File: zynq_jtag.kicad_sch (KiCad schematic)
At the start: 79 parts, among them J300 Digilent HS2 Header, J301 USB-MICRO-B, Q300 T2N7002AK, SW300 SKRPANE010, SW301 219-3LPST, U300 FT2232HL-REEL, U301 93LC56BT-I/SN, U6 XC7Z020-2CLG400I, X300 12Mhz-TXC Corp

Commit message: ram-update
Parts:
- D300, D308, D309: footprint LED_0402_RED -> Footprint-Lib-PhilsLab:LED_0402_RED
- FB300, FB301, FB302: footprint FB_0402 -> Footprint-Lib-PhilsLab:FB_0402
- R310, R312, R314, R316, R319: footprint Resistor_SMD:R_0402_1005Metric -> easyeda2kicad_foorprint:R0201; LCSC C25765 -> C295787; Manufacturer Part Number 0402WGF2002TCE -> RC0201FR-0720KL
- SW300: footprint SKRPANE010 -> Footprint-Lib-PhilsLab:SKRPANE010

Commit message: ram-zynq-updated
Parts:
- D305: footprint Diode_SMD:D_SOD-323F -> easyeda2kicad_foorprint:SOD-323_L1.8-W1.3-LS2.5-RD
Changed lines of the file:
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@@
 			)
 		)
-		(property "Footprint" "Diode_SMD:D_SOD-323F"
+		(property "Footprint" "easyeda2kicad_foorprint:SOD-323_L1.8-W1.3-LS2.5-RD"
 			(at 307.34 67.945 0)
 			(effects

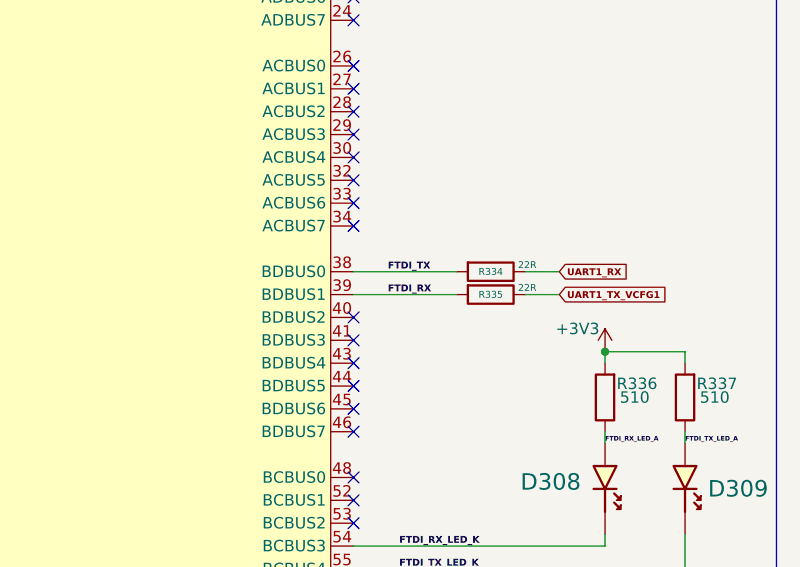
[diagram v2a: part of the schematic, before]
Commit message: usb hs update
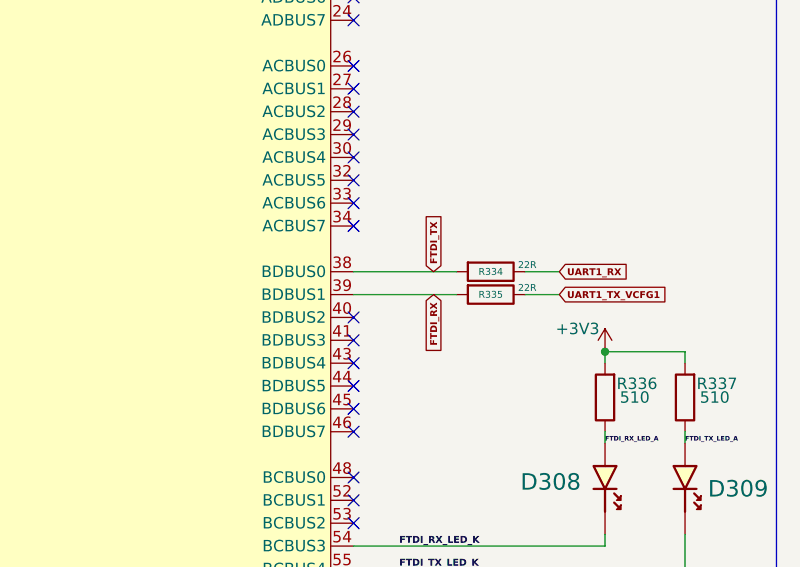
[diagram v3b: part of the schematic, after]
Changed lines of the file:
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@@
-	(wire
-		(pts
-			(xy 444.5 134.62) (xy 433.07 134.62)
-		)
-		(stroke
-			(width 0)
-			(type default)
-		)
-	)
 	(wire
 		(pts
@@
 		(pts
 			(xy 311.15 148.59) (xy 312.42 148.59)
+		)
+		(stroke
+			(width 0)
+			(type default)
+		)
+	)
+	(wire
+		(pts
+			(xy 433.07 134.62) (xy 444.5 134.62)
 		)
 		(stroke
@@
 		)
 	)
-	(label "FTDI_TX"
-		(at 436.88 132.08 0)
-		(fields_autoplaced yes)
-		(effects
-			(font
-				(size 0.762 0.762)
-				(thickness 0.254)
-				(bold yes)
-			)
-			(justify left bottom)
-		)
-	)
 	(label "USB_FTDI_D_N"
 		(at 311.15 104.14 0)
@@
 		)
 	)
-	(label "FTDI_RX"
-		(at 436.88 134.62 0)
-		(fields_autoplaced yes)
-		(effects
-			(font
-				(size 0.762 0.762)
-				(thickness 0.254)
-				(bold yes)
-			)
-			(justify left bottom)
-		)
-	)
 	(label "TMS_0"
 		(at 60.96 50.8 0)
@@
 			)
 			(justify left bottom)
+		)
+	)
+	(global_label "FTDI_RX"
+		(shape input)
+		(at 441.96 134.62 270)
+		(fields_autoplaced yes)
+		(effects
+			(font
+				(size 0.762 0.762)
+				(thickness 0.254)
+				(bold yes)
+			)
+			(justify right)
+		)
+		(property "Intersheetrefs" "${INTERSHEET_REFS}"
+			(at 441.96 141.3143 90)
+			(effects
+				(font
+					(size 1.27 1.27)
+				)
+				(justify right)
+				(hide yes)
+			)
 		)
 	)
@@
 			(effects
 				(font
+					(size 1.27 1.27)
+				)
+				(justify left)
+				(hide yes)
+			)
+		)
+	)
+	(global_label "FTDI_TX"
+		(shape input)
+		(at 441.96 132.08 90)
+		(fields_autoplaced yes)
+		(effects
+			(font
+				(size 0.762 0.762)
+				(thickness 0.254)
+				(bold yes)
+			)
+			(justify left)
+		)
+		(property "Intersheetrefs" "${INTERSHEET_REFS}"
+			(at 441.96 125.5671 90)
+			(effects
+				(font

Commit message: pcb layers
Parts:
- SW300: footprint Footprint-Lib-PhilsLab:SKRPANE010 -> easyeda2kicad_foorprint:SW-SMD_4P-L4.2-W3.2-P2.15-LS4.6-2
- U300: footprint Footprint-Lib-PhilsLab:LQFP-64-0.5mm -> easyeda2kicad_foorprint:LQFP-64_L10.0-W10.0-P0.50-LS12.0-TL
- U301: footprint Footprint-Lib-PhilsLab:SOIC-8 -> easyeda2kicad_foorprint:SOIC-8_L5.0-W4.0-P1.27-LS6.0-BL
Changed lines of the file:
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@@
 			)
 		)
-		(property "Footprint" "Footprint-Lib-PhilsLab:SOIC-8"
+		(property "Footprint" "easyeda2kicad_foorprint:SOIC-8_L5.0-W4.0-P1.27-LS6.0-BL"
 			(at 288.29 165.1 0)
 			(effects
@@
 			)
 		)
-		(property "Footprint" "Footprint-Lib-PhilsLab:LQFP-64-0.5mm"
+		(property "Footprint" "easyeda2kicad_foorprint:LQFP-64_L10.0-W10.0-P0.50-LS12.0-TL"
 			(at 392.43 134.62 0)
 			(effects
@@
 			)
 		)
-		(property "Footprint" "Footprint-Lib-PhilsLab:SKRPANE010"
+		(property "Footprint" "easyeda2kicad_foorprint:SW-SMD_4P-L4.2-W3.2-P2.15-LS4.6-2"
 			(at 173.99 69.85 0)
 			(effects

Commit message: pcbb
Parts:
- SW300: footprint easyeda2kicad_foorprint:SW-SMD_4P-L4.2-W3.2-P2.15-LS4.6-2 -> Footprint-Lib-PhilsLab:SKRPANE010
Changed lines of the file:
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@@
 			)
 		)
-		(property "Footprint" "easyeda2kicad_foorprint:SW-SMD_4P-L4.2-W3.2-P2.15-LS4.6-2"
+		(property "Footprint" "Footprint-Lib-PhilsLab:SKRPANE010"
 			(at 173.99 69.85 0)
 			(effects
